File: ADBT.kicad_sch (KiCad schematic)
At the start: 107 parts, among them J1 ADB1, J2 microUSB, J3 JTAG, Q1 AO3401, Q2 MMBT3904, Q3 MMBT3904, Q4 MMBT3904, Q5 MMBT3904, Q6 AO3401, Q7 AO3401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

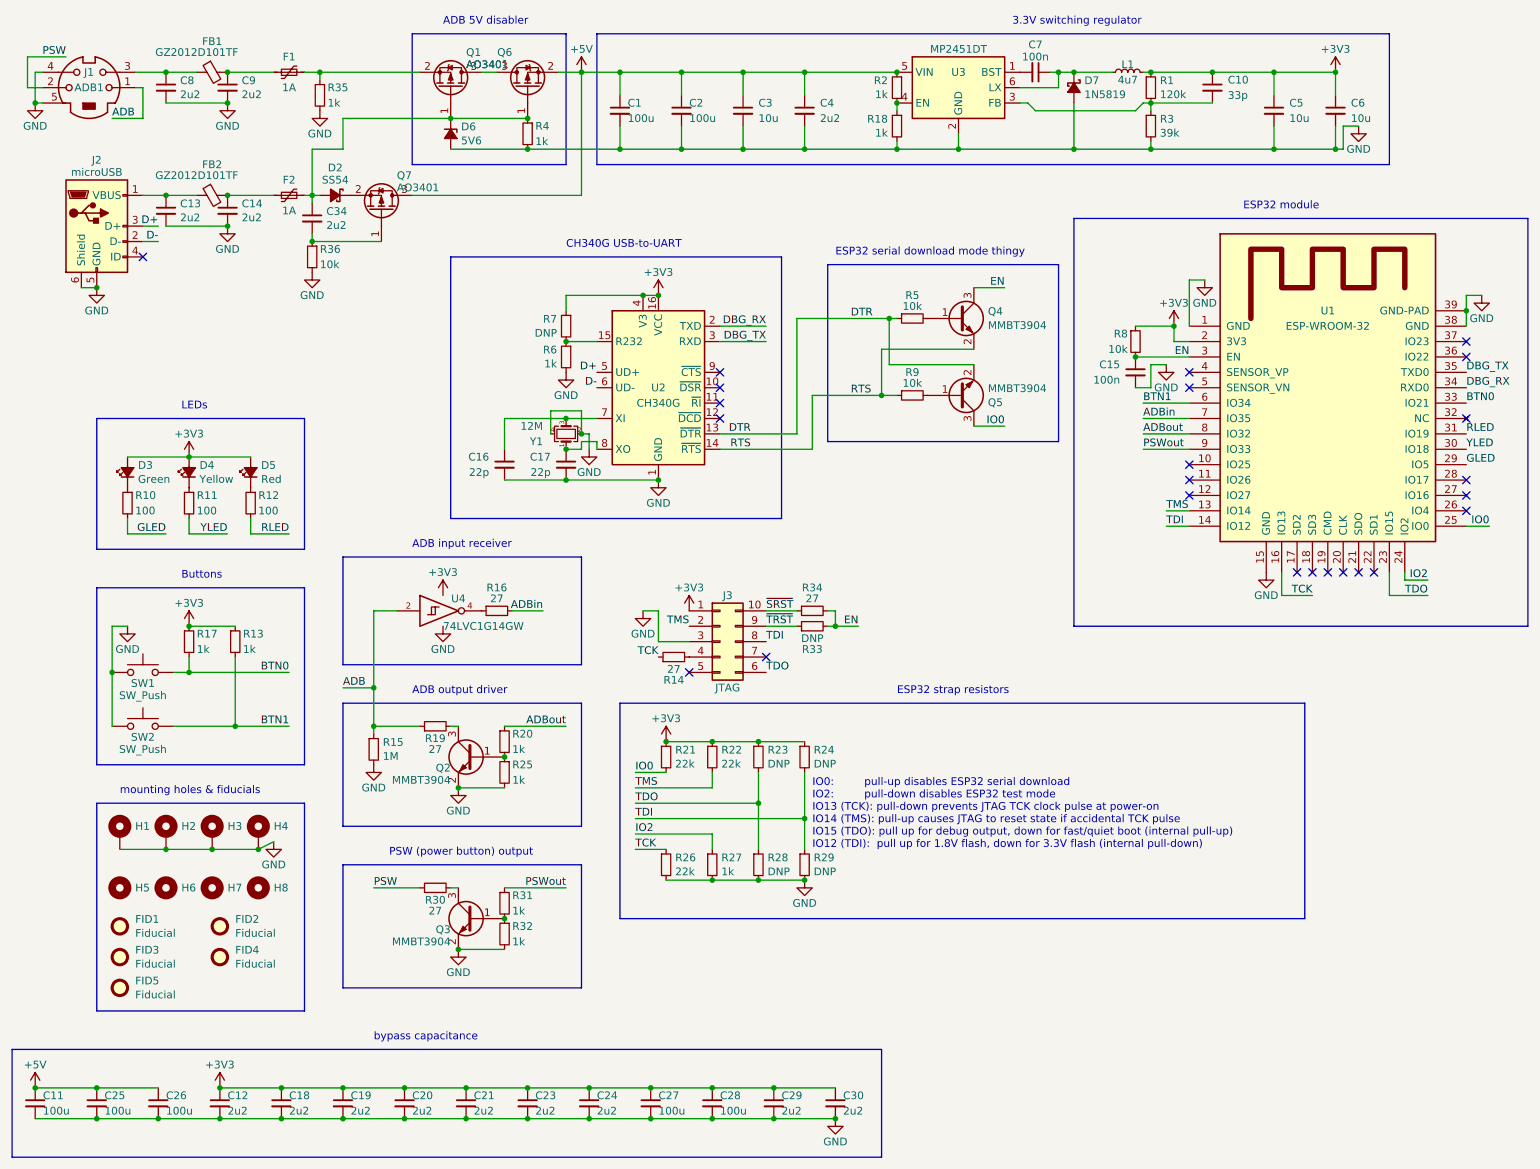
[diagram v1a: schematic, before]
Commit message: New AP3417 regulaor
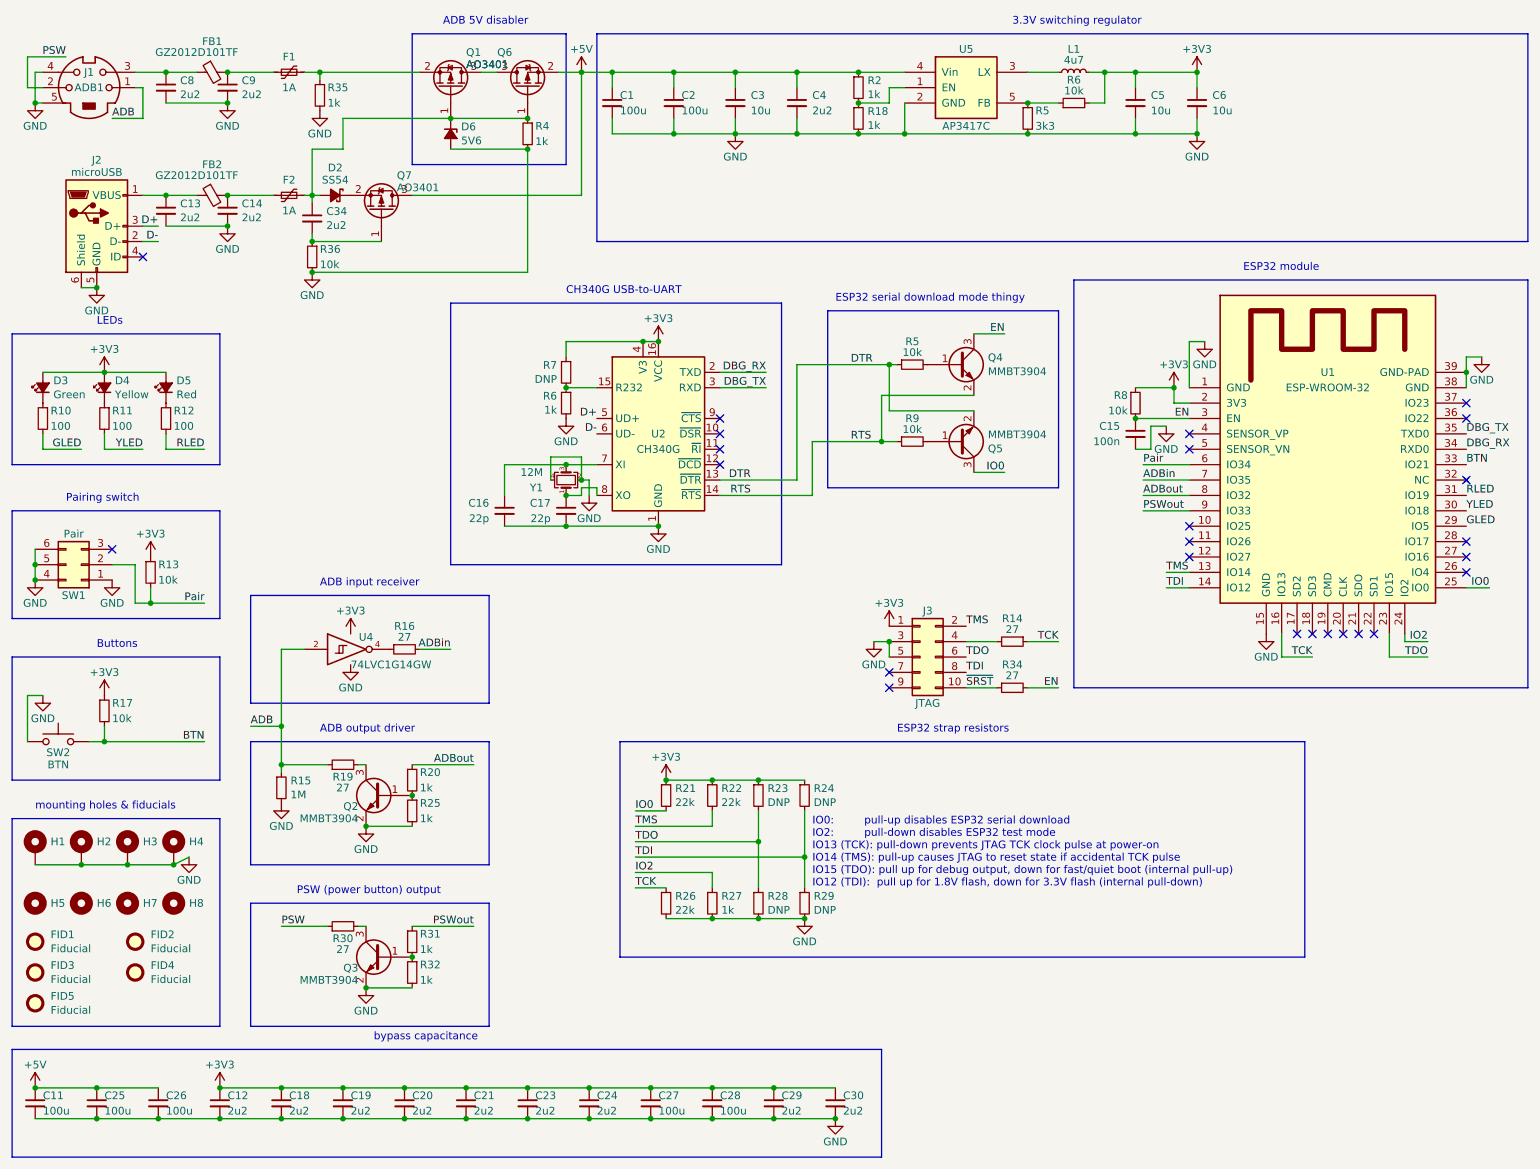
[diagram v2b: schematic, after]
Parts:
- removed C10: 33p, stdpads:C_0603, symbol Device:C_Small
- removed C7: 100n, stdpads:C_0603, symbol Device:C_Small
- removed D7: 1N5819, stdpads:D_SOD-123, symbol Device:D_Schottky_Small_ALT
- removed J3: JTAG, stdpads:Tag-Connect_TC2050-IDC-NL_2x05_P1.27mm_Vertical, symbol Connector_Generic:Conn_02x05_Counter_Clockwise
- removed R1: 120k, stdpads:R_0603, symbol Device:R_Small
- removed R3: 39k, stdpads:R_0603, symbol Device:R_Small
- removed R33: DNP, stdpads:R_0603, symbol Device:R_Small
- removed SW2: SW_Push, stdpads:XKB_TS-1187A, symbol Switch:SW_Push
- removed U3: MP2451DT, stdpads:SOT-23-6, symbol GW_Power:MP2451
- added J3: JTAG, stdpads:Tag-Connect_TC2050-IDC-NL_2x05_P1.27mm_Vertical, symbol Connector_Generic:Conn_02x05_Odd_Even
- added R5: 3k3, stdpads:R_0603, symbol Device:R_Small
- added R6: 10k, stdpads:R_0603, symbol Device:R_Small
- added SW1: Pair, stdpads:SW_CuK_JS202011AQN_DPDT_Angled, symbol Connector_Generic:Conn_02x03_Top_Bottom
- added U5: AP3417C, stdpads:SOT-23-5, symbol GW_Power:AP3417C
- R13, R17: value 1k -> 10k; LCSC Part C21190 -> C25804
- R36: LCSC Part C21190 -> C25804
- SW2: renamed from SW1; value SW_Push -> BTN
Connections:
- net +3V3: now also J3.1 (Pin_1), R6.2
- net +5V: now also U5.4 (Vin)
- net GND: now also J3.3 (Pin_3), J3.5 (Pin_5), R5.2, SW1.1 (Pin_1), SW1.4 (Pin_4), SW1.5 (Pin_5), SW1.6 (Pin_6), U5.2 (GND)
- net TDI: now also J3.8 (Pin_8)
- net TDO: now also J3.6 (Pin_6)
- net TMS: now also J3.2 (Pin_2)
- net ~{SRST}: now also J3.10 (Pin_10)
- net at L1.1: now also U5.3 (LX)
- net at R18.1, R2.2: now also U5.1 (EN)
- net at R14.2: now also J3.4 (Pin_4)
- net BTN0 renamed BTN
- net BTN1 renamed Pair
- net Pair: now also SW1.2 (Pin_2)
- new net: R5.1, R6.1, U5.5 (FB)
- no-connect marks 24 -> 25
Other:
- note added: "Pairing switch"
- moved on the sheet: C1, C15, C16, C17, C2, C3, C4, C5, C6, D3, D4, D5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
